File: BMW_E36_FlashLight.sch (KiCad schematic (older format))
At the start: 6 parts, among them J1 CONN_01X01_FEMALE, J2 CONN_01X01_FEMALE, SW1 SW_DIP_x01

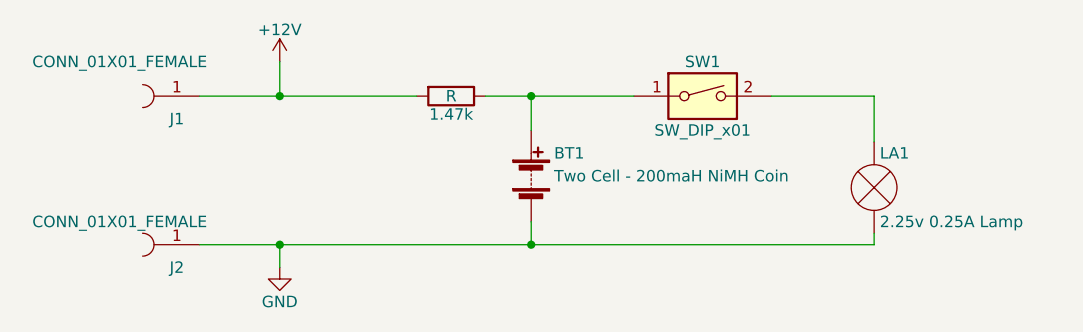
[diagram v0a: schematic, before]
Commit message: Lamp Voltage Rating Change
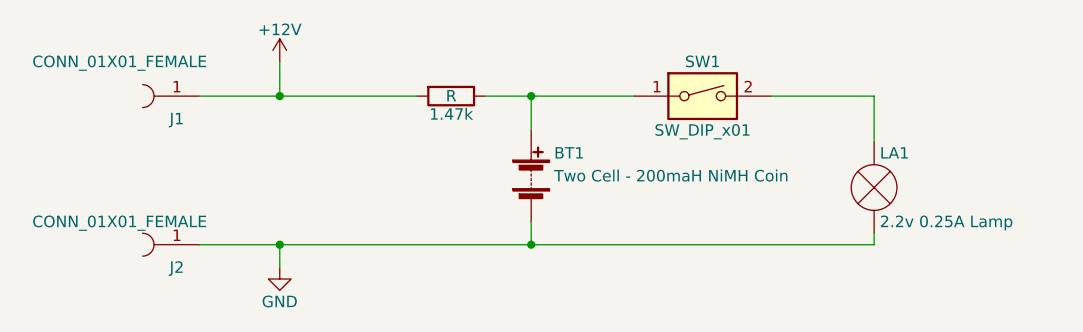
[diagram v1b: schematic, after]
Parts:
- LA1: value 2.25v 0.25A Lamp -> 2.2v 0.25A Lamp
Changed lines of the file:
@@
 P 7100 4100
 F 0 "LA1" H 7125 4250 50  0000 L CNN
-F 1 "2.25v 0.25A Lamp" H 7125 3950 50  0000 L CNN
+F 1 "2.2v 0.25A Lamp" H 7125 3950 50  0000 L CNN
 F 2 "" V 7100 4200 50  0001 C CNN
 F 3 "" V 7100 4200 50  0001 C CNN
